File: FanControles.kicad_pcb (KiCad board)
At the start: 2 copper layers, 29 x 18 mm, 5 parts, among them IC1 PJA3432, P1 24v Fan, P2 24v, P3 100k NTC

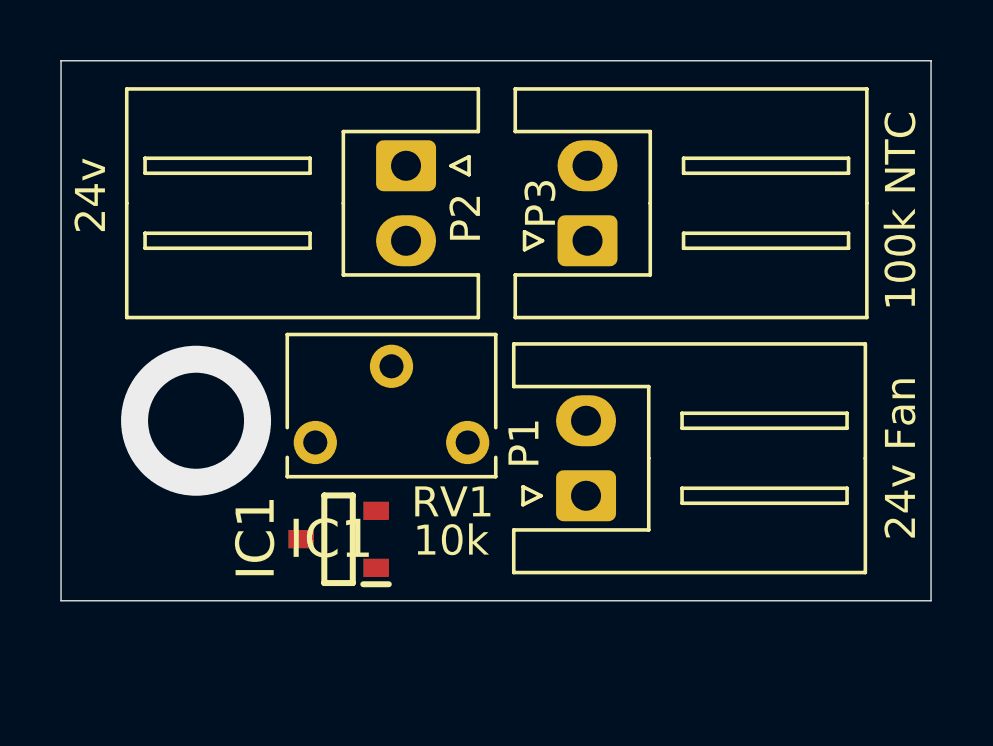
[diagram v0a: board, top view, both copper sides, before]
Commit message: almost done
TODO: change the potenciometer to a cheaper one
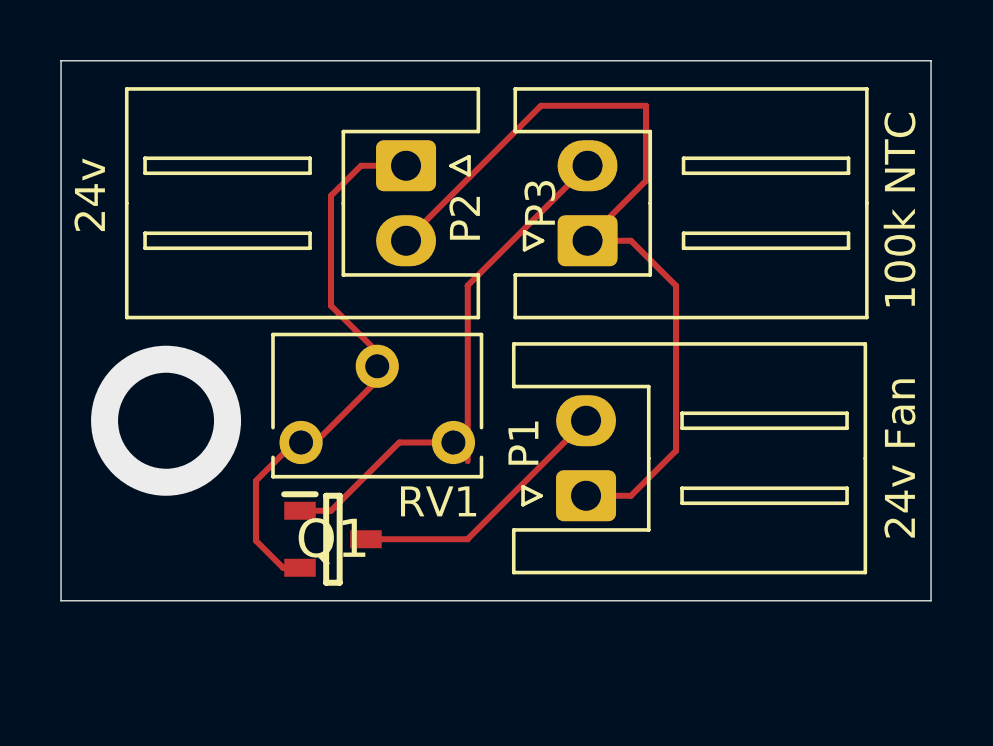
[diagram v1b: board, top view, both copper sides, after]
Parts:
- removed IC1: PJA3432, KiCad:SOT95P240X110-3N
- added Q1: BSH103BKR, BSH:SOT95P230X110-3N, F.Cu at (142.6, 92.5)
- moved RV1 0.47 mm to (141.5, 89.2)
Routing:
- net /+24v: track 0.00 -> 27.9 mm
- net GND: track 0.00 -> 19.5 mm
- net Net-(Q1-G): track 0.00 -> 17.9 mm
- net /Fan: track 0.00 -> 9.14 mm
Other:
- board text added: "WayWayWay"

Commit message: bk
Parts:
- added REF**: MountingHole_3.2mm_M3, MountingHole:MountingHole_3.2mm_M3, F.Cu at (137.0, 89.5)
- moved Q1 2.94 mm to (145.5, 92.5)
- moved RV1 0.50 mm to (142.0, 89.2)
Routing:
- net /Fan: track 9.14 -> 6.06 mm
- net GND: track 19.5 -> 22.3 mm
- net Net-(Q1-G): track 17.9 -> 16.3 mm
- net (no net): vias 1 -> 0
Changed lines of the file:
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@@
 			(outputformat 1)
 			(mirror no)
-			(drillshape 1)
+			(drillshape 0)
 			(scaleselection 1)
-			(outputdirectory "")
+			(outputdirectory "gerbers/")
 		)
 	)
@@
 		)
 	)
+	(footprint "MountingHole:MountingHole_3.2mm_M3"
+		(layer "F.Cu")
+		(at 137 89.5)
+		(descr "Mounting Hole 3.2mm, no annular, M3")
+		(tags "mounting hole 3.2mm no annular m3")
+		(property "Reference" "REF**"
+			(at 0 -4.2 0)
+			(layer "F.SilkS")
+			(effects
+				(font
+					(size 1 1)
+					(thickness 0.15)
+				)
+			)
+		)
+		(property "Value" "MountingHole_3.2mm_M3"
+			(at 0 4.2 0)
+			(layer "F.Fab")
+			(effects
+				(font
+					(size 1 1)
+					(thickness 0.15)
+				)
+			)
+		)
+		(property "Datasheet" ""
+			(at 0 0 0)
+			(unlocked yes)
+			(layer "F.Fab")
+			(hide yes)
+			(effects
+				(font
+					(size 1.27 1.27)
+					(thickness 0.15)
+				)
+			)
+		)
+		(property "Description" ""
+			(at 0 0 0)
+			(unlocked yes)
+			(layer "F.Fab")
+			(hide yes)
+			(effects
+				(font
+					(size 1.27 1.27)
+					(thickness 0.15)
+				)
+			)
+		)
+		(attr exclude_from_pos_files exclude_from_bom)
+		(fp_circle
+			(center 0 0)
+			(end 3.2 0)
+			(stroke
+				(width 0.15)
+				(type solid)
+			)
+			(fill no)
+			(layer "Cmts.User")
+		)
+		(fp_circle
+			(center 0 0)
+			(end 3.45 0)
+			(stroke
+				(width 0.05)
+				(type solid)
+			)
+			(fill no)
+			(layer "F.CrtYd")
+		)
+		(fp_text user "${REFERENCE}"
+			(at 0 0 0)
+			(layer "F.Fab")
+			(effects
+				(font
+					(size 1 1)
+					(thickness 0.15)
+				)
+			)
+		)
+		(pad "" np_thru_hole circle
+			(at 0 0)
+			(size 3.2 3.2)
+			(drill 3.2)
+			(layers "*.Cu" "*.Mask")
+		)
+		(embedded_fonts no)
+	)
 	(footprint "Connector_JST:JST_XH_S2B-XH-A_1x02_P2.50mm_Horizontal"
 		(layer "F.Cu")
@@
 	(footprint "BSH:SOT95P230X110-3N"
 		(layer "F.Cu")
-		(at 142.5625 92.45)
+		(at 145.5 92.5)
 		(descr "SOT23 Nexperia")
 		(tags "MOSFET (N-Channel)")
 		(property "Reference" "Q1"
-			(at 0 0 0)
+			(at 0 3.5 0)
 			(layer "F.SilkS")
 			(effects
@@
 		)
 		(property "Value" "BSH103BKR"
-			(at 0 0 -0)
+			(at 0 0 0)
 			(layer "B.SilkS")
 			(effects
@@
 		)
 		(fp_text user "${REFERENCE}"
-			(at 0 0 0)
+			(at 3.1 3.5 0)
 			(layer "F.Fab")
 			(effects
@@
 	(footprint "Potentiometer_THT:Potentiometer_Bourns_3266W_Vertical"
 		(layer "F.Cu")
-		(at 141.5 89.225 180)
+		(at 142 89.225 180)
 		(descr "Potentiometer, vertical, Bourns 3266W, https://www.bourns.com/docs/Product-Datasheets/3266.pdf")
 		(tags "Potentiometer vertical Bourns 3266W")
@@
 	(dimension
 		(type orthogonal)
-		(layer "Edge.Cuts")
+		(layer "User.1")
 		(pts
 			(xy 162.5 76.5) (xy 133.5 76.5)
@@
 		(gr_text "29"
 			(at 148 72.85 0)
-			(layer "Edge.Cuts")
+			(layer "User.1")
 			(effects
 				(font
@@
 	(dimension
 		(type orthogonal)
-		(layer "Edge.Cuts")
+		(layer "User.1")
 		(pts
 			(xy 162.5 94.5) (xy 162.5 76.5)
@@
 		(gr_text "18"
 			(at 165.35 85.5 90)
-			(layer "Edge.Cuts")
-			(effects
-				(font
-					(size 1 1)
-					(thickness 0.15)
-				)
-			)
-		)
-	)
-	(via
-		(at 137 88.5)
-		(size 5)
-		(drill 3.2)
-		(layers "F.Cu" "B.Cu")
-		(free yes)
-		(net 0)
+			(layer "User.1")
+			(effects
+				(font
+					(size 1 1)
+					(thickness 0.15)
+				)
+			)
+		)
 	)
 	(segment
@@
 	)
 	(segment
-		(start 147.05 92.45)
-		(end 151 88.5)
+		(start 151 88.5)
+		(end 147 92.5)
 		(width 0.2)
 		(layer "F.Cu")
@@
 	)
 	(segment
-		(start 143.5 92.45)
-		(end 147.05 92.45)
+		(start 147 92.5)
+		(end 146.6 92.5)
 		(width 0.2)
 		(layer "F.Cu")
@@
 	)
 	(segment
-		(start 140 90.5)
-		(end 140 92.5)
+		(start 141.5 92)
+		(end 141.5 89.225)
 		(width 0.2)
 		(layer "F.Cu")
@@
 	)
 	(segment
+		(start 142.5 84.67)
+		(end 142.5 81)
+		(width 0.2)
+		(layer "F.Cu")
+		(net 3)
+	)
+	(segment
+		(start 145 87.17)
+		(end 142.5 84.67)
+		(width 0.2)
+		(layer "F.Cu")
+		(net 3)
+	)
+	(segment
+		(start 144.6089 88.824)
+		(end 145 88.824)
+		(width 0.2)
+		(layer "F.Cu")
+		(net 3)
+	)
+	(segment
+		(start 143.5 80)
+		(end 145 80)
+		(width 0.2)
+		(layer "F.Cu")
+		(net 3)
+	)
+	(segment
+		(start 142.725 89.225)
+		(end 143.46645 89.96645)
+		(width 0.2)
+		(layer "F.Cu")
+		(net 3)
+	)
+	(segment
+		(start 144.4 93.45)
+		(end 142.95 93.45)
+		(width 0.2)
+		(layer "F.Cu")
+		(net 3)
+	)
+	(segment
+		(start 145 88.824)
+		(end 145 87.17)
+		(width 0.2)
+		(layer "F.Cu")
+		(net 3)
+	)
+	(segment
+		(start 143.46645 89.96645)
+		(end 144.6089 88.824)
+		(width 0.2)
+		(layer "F.Cu")
+		(net 3)
+	)
+	(segment
+		(start 142.95 93.45)
+		(end 141.5 92)
+		(width 0.2)
+		(layer "F.Cu")
+		(net 3)
+	)
+	(segment
 		(start 142.5 81)
-		(end 142.5 84.67)
+		(end 143.5 80)
 		(width 0.2)
 		(layer "F.Cu")
@@
 	)
 	(segment
-		(start 145 80)
-		(end 143.5 80)
+		(start 141.5 89.225)
+		(end 142.725 89.225)
 		(width 0.2)
 		(layer "F.Cu")
@@
 	)
 	(segment
-		(start 141.275 89.225)
-		(end 140 90.5)
-		(width 0.2)
-		(layer "F.Cu")
-		(net 3)
-	)
-	(segment
-		(start 140 92.5)
-		(end 140.9 93.4)
-		(width 0.2)
-		(layer "F.Cu")
-		(net 3)
-	)
-	(segment
-		(start 141.975 89.225)
-		(end 141.275 89.225)
-		(width 0.2)
-		(layer "F.Cu")
-		(net 3)
-	)
-	(segment
-		(start 143.5 80)
-		(end 142.5 81)
-		(width 0.2)
-		(layer "F.Cu")
-		(net 3)
-	)
-	(segment
-		(start 140.9 93.4)
-		(end 141.625 93.4)
-		(width 0.2)
-		(layer "F.Cu")
-		(net 3)
-	)
-	(segment
-		(start 144.515 86.685)
-		(end 141.975 89.225)
-		(width 0.2)
-		(layer "F.Cu")
-		(net 3)
-	)
-	(segment
-		(start 142.5 84.67)
-		(end 144.515 86.685)
-		(width 0.2)
-		(layer "F.Cu")
-		(net 3)
-	)
-	(segment
-		(start 142.5 91.5)
-		(end 144.775 89.225)
-		(width 0.2)
-		(layer "F.Cu")
-		(net 4)
-	)
-	(segment
-		(start 141.625 91.5)
-		(end 142.5 91.5)
+		(start 144.775 89.225)
+		(end 147.055 89.225)
 		(width 0.2)
 		(layer "F.Cu")
@@
 	)
 	(segment
+		(start 144.4 91.55)
+		(end 144.4 89.6)
+		(width 0.2)
+		(layer "F.Cu")
+		(net 4)
+	)
+	(segment
+		(start 144.4 89.6)
+		(end 144.775 89.225)
+		(width 0.2)
+		(layer "F.Cu")
+		(net 4)
+	)
+	(segment
 		(start 151.05 80)
 		(end 147.055 83.995)
@@
 		(width 0.2)
 		(layer "F.Cu")
-		(net 4)
-	)
-	(segment
-		(start 144.775 89.225)
-		(end 147.055 89.225)
-		(width 0.2)
-		(layer "F.Cu")
